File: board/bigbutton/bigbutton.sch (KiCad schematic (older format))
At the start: 17 parts, among them J1 USB_C_Receptacle_USB2.0, J2 SWD, SW1 ~RST, U1 ATSAMD11C14A-SS, U2 ATECC608A-SSHDA, U3 WE-TVS-82400102, X1 16MHz

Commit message: Start moving to STM32
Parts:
- removed R3: 1kΩ, symbol Device:R_Small
- removed U1: ATSAMD11C14A-SS, Package_SO:SOIC-14_3.9x8.7mm_P1.27mm, symbol MCU_Microchip_SAMD:ATSAMD11C14A-SS
- added C5, C6 (x2), C7, C8: 0.1µF, symbol Device:C_Small
- added R7, R8: 10kΩ, symbol Device:R_Small
- added TP_3V3, TP_5V0, TP_CC1, TP_CC2, TP_GND1, TP_SCL1, TP_SDA1, TP_SWCLK1, TP_SWDIO1, TP_~RST1: TestPoint, symbol Connector:TestPoint
- added U4: STM32F302CBTx, Package_QFP:LQFP-48_7x7mm_P0.5mm, symbol MCU_ST_STM32F3:STM32F302CBTx
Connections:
- net labels added: I2C_SCL, I2C_SDA, MCU_DIN, MCU_DOUT, MCU_SCK, USB_CC1, USB_CC2
- no-connect marks 2 -> 4
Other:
- moved on the sheet: R4, R5, U2

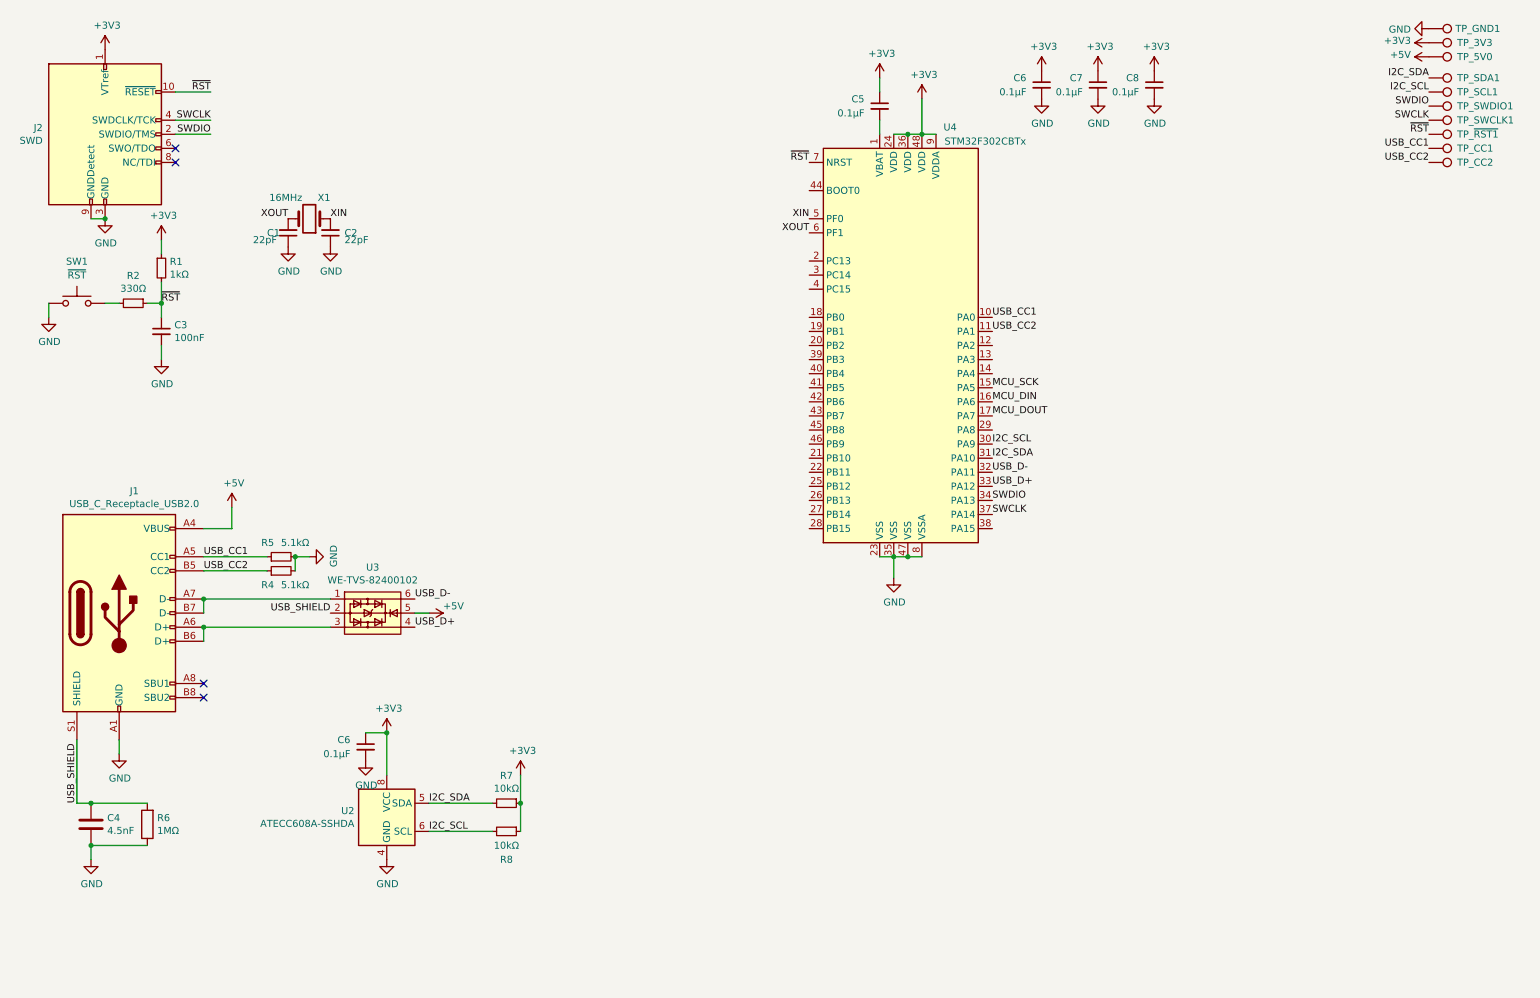
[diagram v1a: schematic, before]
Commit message: Add LEDs and create a symbol for level shifter
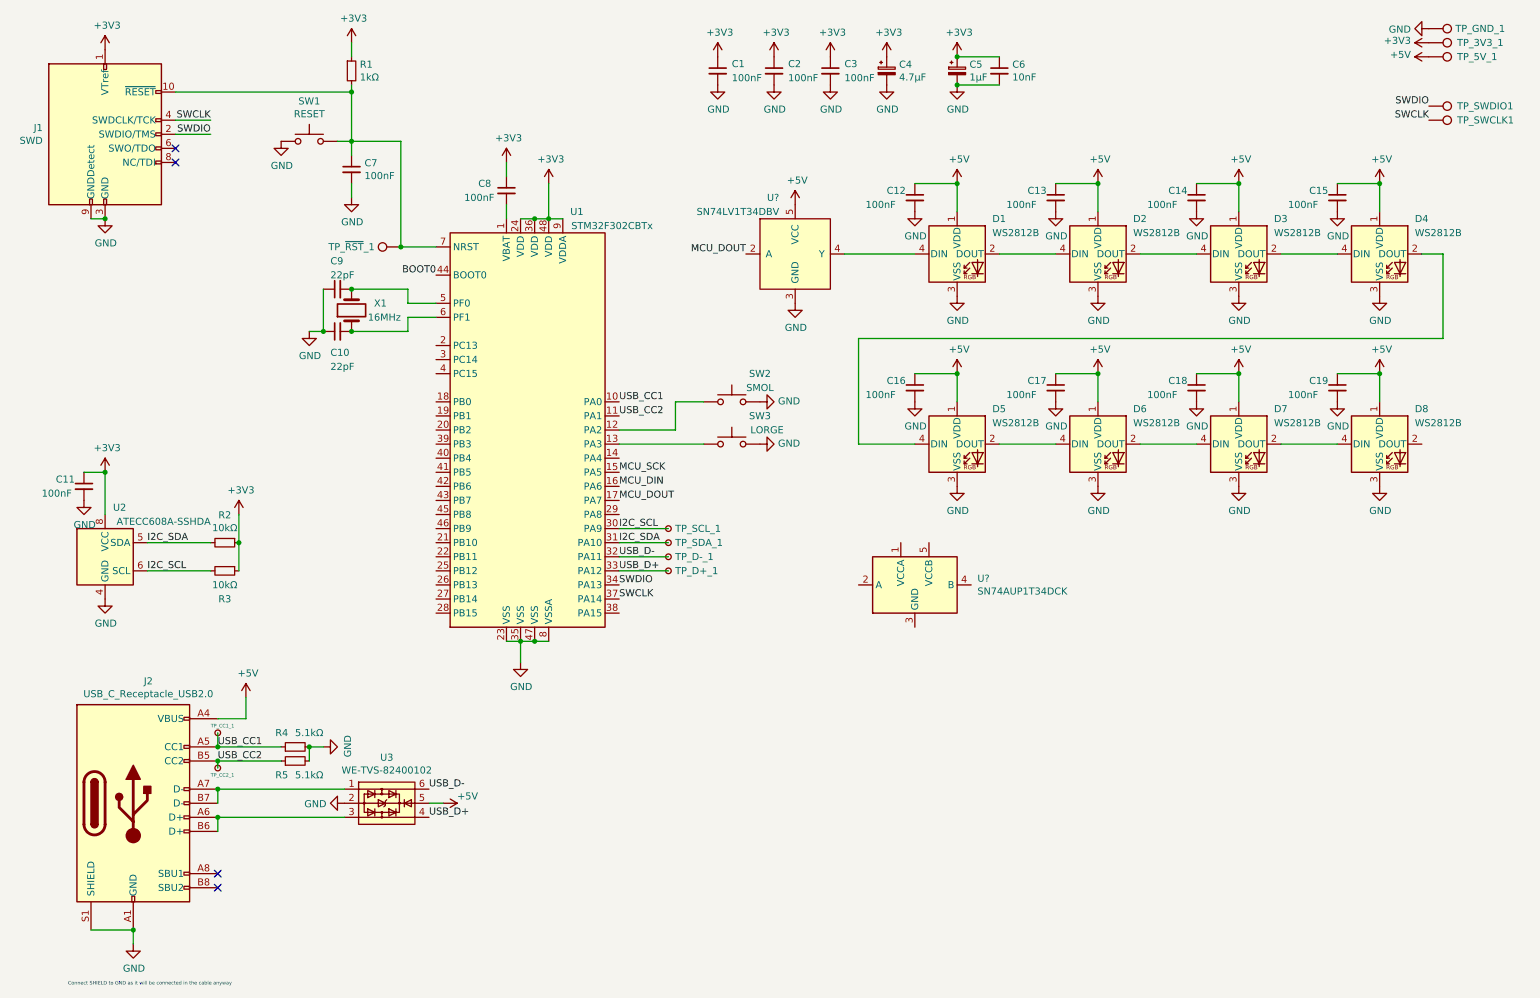
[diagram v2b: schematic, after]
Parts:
- removed C4: 4.5nF, symbol Device:C
- removed R2: 330Ω, symbol Device:R_Small
- removed R6: 1MΩ, symbol Device:R
- removed TP_CC1, TP_CC2, TP_SCL1, TP_SDA1, TP_~RST1: TestPoint, symbol Connector:TestPoint
- added C12, C13, C14, C15, C16, C17, C18, C19: 100nF, Capacitor_SMD:C_0603_1608Metric_Pad1.05x0.95mm_HandSolder, symbol Device:C_Small
- added C4: 4.7µF, Capacitor_SMD:C_0603_1608Metric_Pad1.05x0.95mm_HandSolder, symbol Device:CP_Small
- added C5: 1µF, Capacitor_SMD:C_0603_1608Metric_Pad1.05x0.95mm_HandSolder, symbol Device:CP_Small
- added C6: 10nF, Capacitor_SMD:C_0603_1608Metric_Pad1.05x0.95mm_HandSolder, symbol Device:C_Small
- added D1, D2, D3, D4, D5, D6, D7, D8: WS2812B, LED_SMD:LED_WS2812B_PLCC4_5.0x5.0mm_P3.2mm, symbol LED:WS2812B
- added SW2: SMOL, Button_Switch_Keyboard:SW_Cherry_MX_1.00u_PC, symbol Switch:SW_Push
- added SW3: LORGE, Button_Switch_Keyboard:SW_Cherry_MX_1.00u_PC, symbol Switch:SW_Push
- added TP_CC1_1: TP_CC1, symbol Connector:TestPoint_Small
- added TP_CC2_1: TP_CC2, symbol Connector:TestPoint_Small
- added TP_D+_1, TP_D-_1, TP_SCL_1, TP_SDA_1: TestPoint_Small, symbol Connector:TestPoint_Small
- added TP_~RST~_1: TestPoint, symbol Connector:TestPoint
- added U?: SN74AUP1T34DCK, Package_TO_SOT_SMD:SOT-353_SC-70-5, symbol Logic_LevelTranslator:SN74AUP1T34DCK
- added U?: SN74LV1T34DBV, Package_TO_SOT_SMD:SOT-23-5, symbol bigbutton:SN74LV1T34DBV
- C1, C11: renamed from C6; value 0.1µF -> 100nF; footprint (none) -> Capacitor_SMD:C_0603_1608Metric_Pad1.05x0.95mm_HandSolder
- C10: renamed from C2; footprint Capacitor_SMD:C_0805_2012Metric_Pad1.15x1.40mm_HandSolder -> Capacitor_SMD:C_0603_1608Metric_Pad1.05x0.95mm_HandSolder
- C2: renamed from C7; value 0.1µF -> 100nF; footprint (none) -> Capacitor_SMD:C_0603_1608Metric_Pad1.05x0.95mm_HandSolder
- C3: renamed from C8; value 0.1µF -> 100nF; footprint (none) -> Capacitor_SMD:C_0603_1608Metric_Pad1.05x0.95mm_HandSolder
- C7: renamed from C3; footprint (none) -> Capacitor_SMD:C_0603_1608Metric_Pad1.05x0.95mm_HandSolder
- C8: renamed from C5; value 0.1µF -> 100nF; footprint (none) -> Capacitor_SMD:C_0603_1608Metric_Pad1.05x0.95mm_HandSolder
- C9: renamed from C1; footprint Capacitor_SMD:C_0805_2012Metric_Pad1.15x1.40mm_HandSolder -> Capacitor_SMD:C_0603_1608Metric_Pad1.05x0.95mm_HandSolder
- R1: footprint (none) -> Resistor_SMD:R_0603_1608Metric_Pad1.05x0.95mm_HandSolder
- R2: renamed from R7; footprint (none) -> Resistor_SMD:R_0603_1608Metric_Pad1.05x0.95mm_HandSolder
- R3: renamed from R8; footprint (none) -> Resistor_SMD:R_0603_1608Metric_Pad1.05x0.95mm_HandSolder
- R4: renamed from R5; footprint (none) -> Resistor_SMD:R_0603_1608Metric_Pad1.05x0.95mm_HandSolder
- R5: renamed from R4; footprint (none) -> Resistor_SMD:R_0603_1608Metric_Pad1.05x0.95mm_HandSolder
- SW1: value ~RST -> RESET
- renumbered J2 to J1, J1 to J2, TP_3V3 to TP_3V3_1, TP_5V0 to TP_5V_1, TP_GND1 to TP_GND_1, U4 to U1
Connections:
- net USB_SHIELD is gone; now on net GND: J2.S1 (SHIELD), U3.2
- net ~RST is gone; now on an unnamed net: C7.1, J1.10 (~RESET~), R1.2, U1.7 (NRST)
- net +3V3: now also C4.1, C5.1, C6.1
- net +5V: now also C12.1, C13.1, C14.1, C15.1, C16.1, C17.1, C18.1, C19.1, D1.1 (VDD), D2.1 (VDD), D3.1 (VDD), D4.1 (VDD), D5.1 (VDD), D6.1 (VDD), D7.1 (VDD), D8.1 (VDD), U?.5 (VCC)
- net GND: now also C12.2, C13.2, C14.2, C15.2, C16.2, C17.2, C18.2, C19.2, C4.2, C5.2, C6.2, D1.3 (VSS), D2.3 (VSS), D3.3 (VSS), D4.3 (VSS), D5.3 (VSS), D6.3 (VSS), D7.3 (VSS), D8.3 (VSS), SW2.2, SW3.2, U?.3 (GND)
- net I2C_SCL: now also TP_SCL_1.1
- net I2C_SDA: now also TP_SDA_1.1
- net MCU_DOUT: now also U?.2 (A)
- net USB_CC1: now also TP_CC1_1.1
- net USB_CC2: now also TP_CC2_1.1
- net USB_D+: now also TP_D+_1.1
- net USB_D-: now also TP_D-_1.1
- net at SW1.2: now also TP_~RST~_1.1
- net at U1.12 (PA2): now also SW2.1
- net at U1.13 (PA3): now also SW3.1
- net BOOT0: now reaches U1.44 (BOOT0)
- net XIN: no longer names the net of C10.2, X1.1
- net XIN: now also U1.6 (PF1); no longer U1.5 (PF0)
- net XOUT: no longer names the net of C9.2, X1.2
- net XOUT: now also U1.5 (PF0); no longer U1.6 (PF1)
- new net: D1.2 (DOUT), D2.4 (DIN)
- new net: D1.4 (DIN), U?.4 (Y)
- new net: D2.2 (DOUT), D3.4 (DIN)
- new net: D3.2 (DOUT), D4.4 (DIN)
- new net: D4.2 (DOUT), D5.4 (DIN)
- new net: D5.2 (DOUT), D6.4 (DIN)
- new net: D6.2 (DOUT), D7.4 (DIN)
- new net: D7.2 (DOUT), D8.4 (DIN)
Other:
- note added: "Connect SHIELD to GND as it will be connected in the cable anyway"
- moved on the sheet: C1, C10, C11, C2, C3, C7, C8, C9, J2, R1, R2, R3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

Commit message: Add vreg
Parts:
- removed TP_3V3_1, TP_5V_1, TP_GND_1, TP_SWCLK1, TP_SWDIO1: TestPoint, symbol Connector:TestPoint
- removed U?: SN74AUP1T34DCK, Package_TO_SOT_SMD:SOT-353_SC-70-5, symbol Logic_LevelTranslator:SN74AUP1T34DCK
- added C? (x2): 1µF, symbol Device:C_Small
- added TP_3V3_1, TP_5V_1, TP_GND_1: TestPoint_Small, symbol Connector:TestPoint_Small
- added U?: MIC5501-3.3YM5, Package_TO_SOT_SMD:SOT-23-5, symbol Regulator_Linear:MIC5501-3.0YM5
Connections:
- net +3V3: now also C?.1, TP_3V3_1.1, U?.5 (VOUT)
- net +5V: now also C?.1, TP_5V_1.1, U?.1 (VIN), U?.3 (EN)
- net GND: now also C?.2, C?.2, TP_GND_1.1, U?.2 (GND)
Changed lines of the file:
@@
 Text Label 4800 4150 0    50   ~ 0
 I2C_SCL
-$Comp
-L Connector:TestPoint TP_SWDIO1
-U 1 1 5F610285
-P 10550 1150
-F 0 "TP_SWDIO1" V 10550 1350 50  0000 L CNN
-F 1 "TestPoint" V 10595 1338 50  0001 L CNN
-F 2 "" H 10750 1150 50  0001 C CNN
-F 3 "~" H 10750 1150 50  0001 C CNN
-	1    10550 1150
-	0    1    1    0
-$EndComp
-$Comp
-L Connector:TestPoint TP_SWCLK1
-U 1 1 5F610307
-P 10550 1250
-F 0 "TP_SWCLK1" V 10550 1450 50  0000 L CNN
-F 1 "TestPoint" V 10595 1438 50  0001 L CNN
-F 2 "" H 10750 1250 50  0001 C CNN
-F 3 "~" H 10750 1250 50  0001 C CNN
-	1    10550 1250
-	0    1    1    0
-$EndComp
-Text Label 10550 1150 2    50   ~ 0
-SWDIO
-Text Label 10550 1250 2    50   ~ 0
-SWCLK
 Text Label 4800 4350 0    50   ~ 0
 USB_D-
@@
 Text Label 4800 3750 0    50   ~ 0
 MCU_SCK
-$Comp
-L Connector:TestPoint TP_GND_1
-U 1 1 5F63CA5F
-P 10550 600
-F 0 "TP_GND_1" V 10550 788 50  0000 L CNN
-F 1 "TestPoint" V 10595 788 50  0001 L CNN
-F 2 "" H 10750 600 50  0001 C CNN
-F 3 "~" H 10750 600 50  0001 C CNN
-	1    10550 600
-	0    1    1    0
-$EndComp
-$Comp
-L power:GND #PWR01
-U 1 1 5F63D061
-P 10550 600
-F 0 "#PWR01" H 10550 350 50  0001 C CNN
-F 1 "GND" V 10555 472 50  0000 R CNN
-F 2 "" H 10550 600 50  0001 C CNN
-F 3 "" H 10550 600 50  0001 C CNN
-	1    10550 600
-	0    1    1    0
-$EndComp
-$Comp
-L Connector:TestPoint TP_3V3_1
-U 1 1 5F63F10F
-P 10550 700
-F 0 "TP_3V3_1" V 10550 900 50  0000 L CNN
-F 1 "TestPoint" V 10595 888 50  0001 L CNN
-F 2 "" H 10750 700 50  0001 C CNN
-F 3 "~" H 10750 700 50  0001 C CNN
-	1    10550 700
-	0    1    1    0
-$EndComp
-$Comp
-L power:+3V3 #PWR03
-U 1 1 5F63F709
-P 10550 700
-F 0 "#PWR03" H 10550 550 50  0001 C CNN
-F 1 "+3V3" V 10565 828 50  0000 L CNN
-F 2 "" H 10550 700 50  0001 C CNN
-F 3 "" H 10550 700 50  0001 C CNN
-	1    10550 700
-	0    -1   -1   0
-$EndComp
-$Comp
-L Connector:TestPoint TP_5V_1
-U 1 1 5F63F82F
-P 10550 800
-F 0 "TP_5V_1" V 10550 1000 50  0000 L CNN
-F 1 "TestPoint" V 10595 988 50  0001 L CNN
-F 2 "" H 10750 800 50  0001 C CNN
-F 3 "~" H 10750 800 50  0001 C CNN
-	1    10550 800
-	0    1    1    0
-$EndComp
-$Comp
-L power:+5V #PWR09
-U 1 1 5F63FFC3
-P 10550 800
-F 0 "#PWR09" H 10550 650 50  0001 C CNN
-F 1 "+5V" V 10565 928 50  0000 L CNN
-F 2 "" H 10550 800 50  0001 C CNN
-F 3 "" H 10550 800 50  0001 C CNN
-	1    10550 800
-	0    -1   -1   0
-$EndComp
 Wire Wire Line
 	4100 1950 4200 1950
@@
 	6400 2200 6900 2200
 $Comp
-L Logic_LevelTranslator:SN74AUP1T34DCK U?
-U 1 1 5F79F9D3
-P 6900 4550
-F 0 "U?" H 7344 4596 50  0000 L CNN
-F 1 "SN74AUP1T34DCK" H 7344 4505 50  0000 L CNN
-F 2 "Package_TO_SOT_SMD:SOT-353_SC-70-5" H 6900 3850 50  0001 C CNN
-F 3 "http://www.ti.com/lit/ds/symlink/sn74aup1t34.pdf" H 6900 3950 50  0001 C CNN
-	1    6900 4550
-	1    0    0    -1
-$EndComp
-$Comp
 L bigbutton:SN74LV1T34DBV U?
 U 1 1 5F7A4DA0
@@
 	1    0    0    -1
 $EndComp
+$Comp
+L Regulator_Linear:MIC5501-3.0YM5 U?
+U 1 1 5F7ACD40
+P 5100 6500
+F 0 "U?" H 5100 6867 50  0000 C CNN
+F 1 "MIC5501-3.3YM5" H 5100 6776 50  0000 C CNN
+F 2 "Package_TO_SOT_SMD:SOT-23-5" H 5100 6100 50  0001 C CNN
+F 3 "http://ww1.microchip.com/downloads/en/DeviceDoc/MIC550X.pdf" H 4850 6750 50  0001 C CNN
+	1    5100 6500
+	1    0    0    -1
+$EndComp
+Wire Wire Line
+	4700 6400 4700 6600
+Wire Wire Line
+	4700 6400 4500 6400
+Wire Wire Line
+	4500 6400 4500 6300
+Connection ~ 4700 6400
+$Comp
+L power:+5V #PWR?
+U 1 1 5F7B4962
+P 4500 6300
+F 0 "#PWR?" H 4500 6150 50  0001 C CNN
+F 1 "+5V" H 4515 6473 50  0000 C CNN
+F 2 "" H 4500 6300 50  0001 C CNN
+F 3 "" H 4500 6300 50  0001 C CNN
+	1    4500 6300
+	1    0    0    -1
+$EndComp
+Wire Wire Line
+	5500 6400 5700 6400
+Wire Wire Line
+	5700 6400 5700 6300
+$Comp
+L power:+3V3 #PWR?
+U 1 1 5F7B7EC3
+P 5700 6300
+F 0 "#PWR?" H 5700 6150 50  0001 C CNN
+F 1 "+3V3" H 5715 6473 50  0000 C CNN
+F 2 "" H 5700 6300 50  0001 C CNN
+F 3 "" H 5700 6300 50  0001 C CNN
+	1    5700 6300
+	1    0    0    -1
+$EndComp
+$Comp
+L power:GND #PWR?
+U 1 1 5F7B8883
+P 5100 6800
+F 0 "#PWR?" H 5100 6550 50  0001 C CNN
+F 1 "GND" H 5105 6627 50  0000 C CNN
+F 2 "" H 5100 6800 50  0001 C CNN
+F 3 "" H 5100 6800 50  0001 C CNN
+	1    5100 6800
+	1    0    0    -1
+$EndComp
+$Comp
+L Device:C_Small C?
+U 1 1 5F7B9C07
+P 4500 6500
+F 0 "C?" H 4300 6550 50  0000 L CNN
+F 1 "1µF" H 4250 6450 50  0000 L CNN
+F 2 "" H 4500 6500 50  0001 C CNN
+F 3 "~" H 4500 6500 50  0001 C CNN
+	1    4500 6500
+	1    0    0    -1
+$EndComp
+Connection ~ 4500 6400
+Wire Wire Line
+	4500 6600 4500 6800
+Wire Wire Line
+	4500 6800 5100 6800
+Connection ~ 5100 6800
+Wire Wire Line
+	5100 6800 5700 6800
+Wire Wire Line
+	5700 6800 5700 6600
+$Comp
+L Device:C_Small C?
+U 1 1 5F7C0E99
+P 5700 6500
+F 0 "C?" H 5792 6546 50  0000 L CNN
+F 1 "1µF" H 5792 6455 50  0000 L CNN
+F 2 "" H 5700 6500 50  0001 C CNN
+F 3 "~" H 5700 6500 50  0001 C CNN
+	1    5700 6500
+	1    0    0    -1
+$EndComp
+Connection ~ 5700 6400
+$Comp
+L Connector:TestPoint_Small TP_5V_1
+U 1 1 5F7C43D8
+P 4400 6300
+F 0 "TP_5V_1" H 4050 6300 50  0000 L CNN
+F 1 "TestPoint_Small" H 4448 6255 50  0001 L CNN
+F 2 "" H 4600 6300 50  0001 C CNN
+F 3 "~" H 4600 6300 50  0001 C CNN
+	1    4400 6300
+	1    0    0    -1
+$EndComp
+Wire Wire Line
+	4400 6300 4400 6400
+Wire Wire Line
+	4400 6400 4500 6400
+$Comp
+L Connector:TestPoint_Small TP_GND_1
+U 1 1 5F7C7F7F
+P 4500 6900
+F 0 "TP_GND_1" H 4548 6900 50  0000 L CNN
+F 1 "TestPoint_Small" H 4548 6855 50  0001 L CNN
+F 2 "" H 4700 6900 50  0001 C CNN
+F 3 "~" H 4700 6900 50  0001 C CNN
+	1    4500 6900
+	1    0    0    -1
+$EndComp
+Wire Wire Line
+	4500 6800 4500 6900
+Connection ~ 4500 6800
+$Comp
+L Connector:TestPoint_Small TP_3V3_1
+U 1 1 5F7CBAA6
+P 5800 6300
+F 0 "TP_3V3_1" H 5848 6300 50  0000 L CNN
+F 1 "TestPoint_Small" H 5848 6255 50  0001 L CNN
+F 2 "" H 6000 6300 50  0001 C CNN
+F 3 "~" H 6000 6300 50  0001 C CNN
+	1    5800 6300
+	1    0    0    -1
+$EndComp
+Wire Wire Line
+	5800 6300 5800 6400
+Wire Wire Line
+	5800 6400 5700 6400
 $EndSCHEMATC
